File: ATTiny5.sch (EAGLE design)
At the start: 20 parts, among them Q1 BSP100, U1 SPX5205M5-L-3-3, U2 ATTINY5-TSHR, X1 DIODES, X2 INPUT

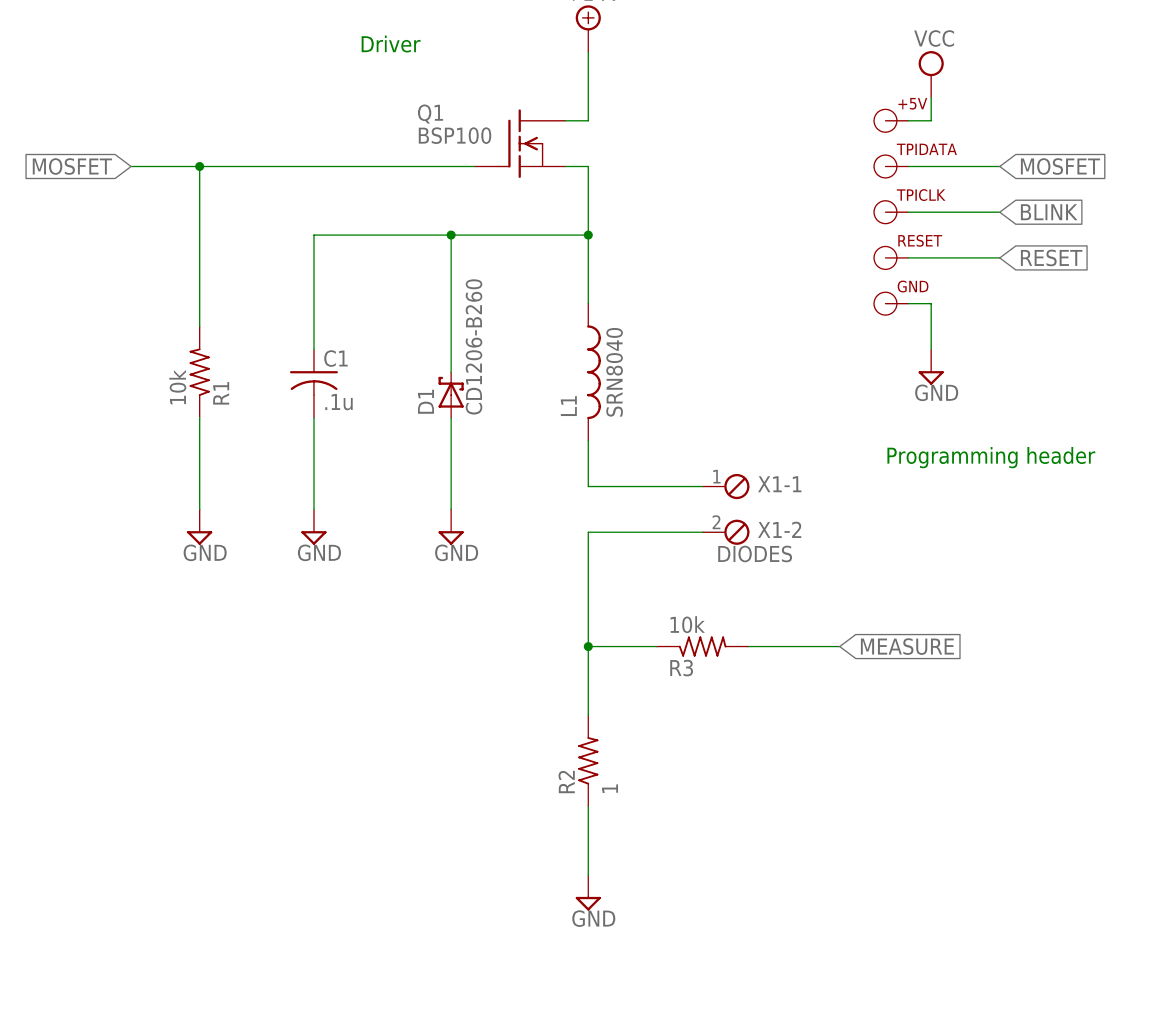
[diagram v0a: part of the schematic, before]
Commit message: Updated Board
Updated Board with Optional current limiting transistor and properly
sized and connected output cap.
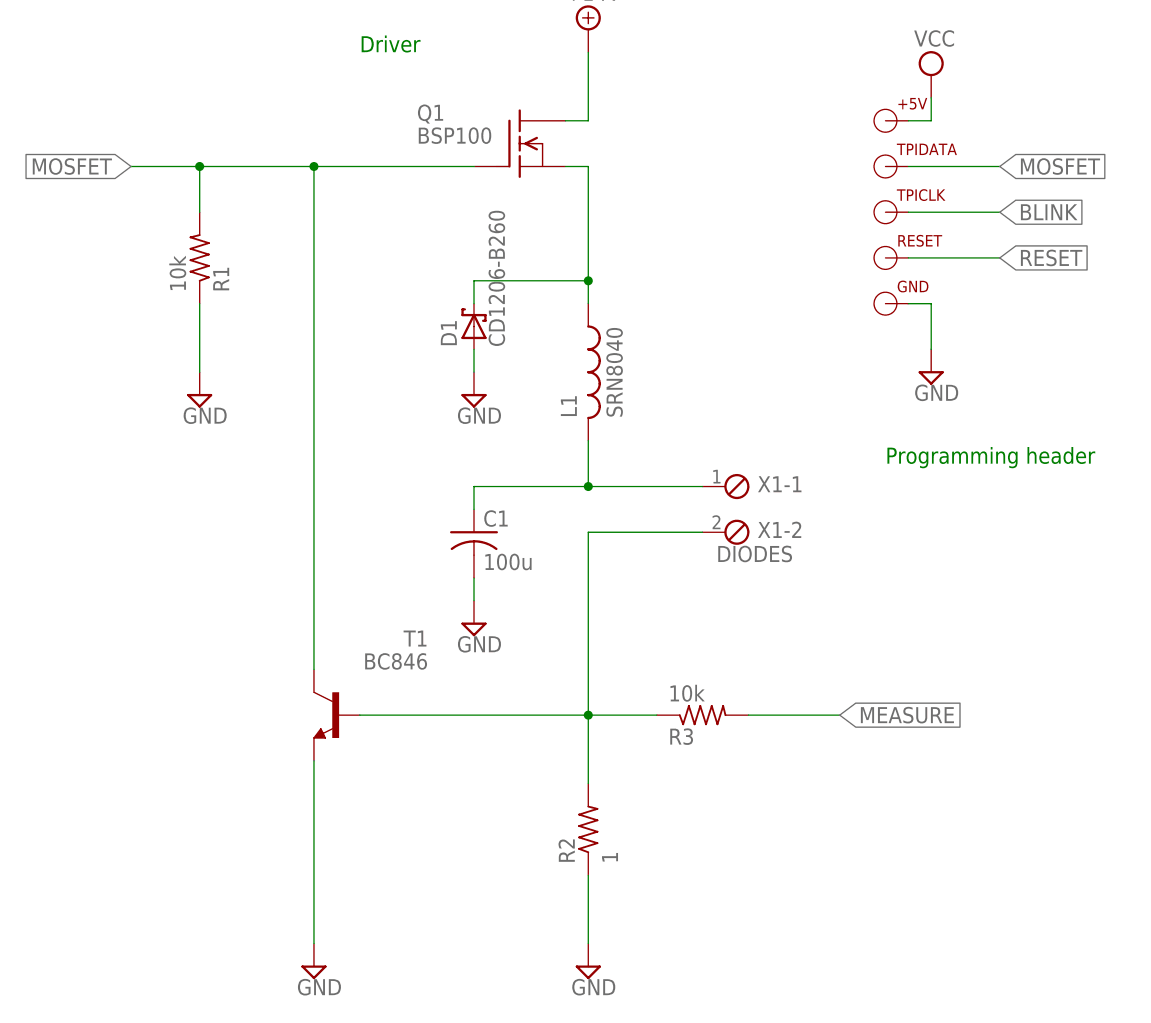
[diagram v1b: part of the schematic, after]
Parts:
- added T1: BC846, transistor:BC846
- C1: value .1u -> 100u; device resistor:C-USC0805 -> Personal:AVE107M25X16T-F
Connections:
- net D-: now also T1.B
- net GND: now also C1.C-, T1.E; no longer C1.2
- net L+: no longer C1.1
- net MOSFET: now also T1.C
- net N$3: now also C1.C+
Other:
- moved on the sheet: C1, D1, R1, R2, R3
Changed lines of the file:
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@@
 <part name="SUPPLY10" library="supply2" deviceset="GND" device=""/>
 <part name="SUPPLY12" library="supply2" deviceset="GND" device=""/>
-<part name="C1" library="resistor" deviceset="C-US" device="C0805" value=".1u"/>
+<part name="C1" library="Personal" deviceset="AVE107M25X16T-F" device="" value="100u"/>
 <part name="SUPPLY13" library="supply2" deviceset="GND" device=""/>
 <part name="R1" library="resistor" deviceset="R-US_" device="R1206" value="10k"/>
@@
 <part name="SUPPLY17" library="supply2" deviceset="GND" device=""/>
 <part name="RESET" library="Personal" deviceset="TPI" device=""/>
+<part name="T1" library="transistor" deviceset="BC846" device=""/>
+<part name="SUPPLY18" library="supply2" deviceset="GND" device=""/>
 </parts>
 <sheets>
@@
 <instance part="SUPPLY6" gate="G$1" x="139.7" y="165.1"/>
 <instance part="SUPPLY7" gate="GND" x="139.7" y="147.32"/>
-<instance part="R2" gate="G$1" x="81.28" y="33.02" rot="R90"/>
-<instance part="SUPPLY8" gate="GND" x="81.28" y="17.78"/>
+<instance part="R2" gate="G$1" x="81.28" y="25.4" rot="R90"/>
+<instance part="SUPPLY8" gate="GND" x="81.28" y="10.16"/>
 <instance part="X1" gate="-1" x="96.52" y="63.5"/>
 <instance part="X1" gate="-2" x="96.52" y="58.42"/>
@@
 <instance part="SUPPLY11" gate="G$1" x="81.28" y="114.3"/>
 <instance part="U2" gate="A" x="170.18" y="160.02"/>
-<instance part="R3" gate="G$1" x="93.98" y="45.72" rot="MR180"/>
+<instance part="R3" gate="G$1" x="93.98" y="38.1" rot="MR180"/>
 <instance part="L1" gate="G$1" x="81.28" y="76.2"/>
-<instance part="D1" gate="G$1" x="66.04" y="73.66" rot="R90"/>
+<instance part="D1" gate="G$1" x="68.58" y="81.28" rot="R90"/>
 <instance part="SUPPLY9" gate="G$1" x="43.18" y="172.72"/>
 <instance part="R4" gate="G$1" x="182.88" y="101.6" rot="R180"/>
 <instance part="R5" gate="G$1" x="195.58" y="93.98" rot="R270"/>
 <instance part="SUPPLY10" gate="GND" x="195.58" y="83.82"/>
-<instance part="SUPPLY12" gate="GND" x="66.04" y="58.42"/>
-<instance part="C1" gate="G$1" x="50.8" y="76.2"/>
-<instance part="SUPPLY13" gate="GND" x="50.8" y="58.42"/>
-<instance part="R1" gate="G$1" x="38.1" y="76.2" rot="MR90"/>
-<instance part="SUPPLY14" gate="GND" x="38.1" y="58.42"/>
+<instance part="SUPPLY12" gate="GND" x="68.58" y="73.66"/>
+<instance part="C1" gate="G$1" x="68.58" y="58.42"/>
+<instance part="SUPPLY13" gate="GND" x="68.58" y="48.26"/>
+<instance part="R1" gate="G$1" x="38.1" y="88.9" rot="MR90"/>
+<instance part="SUPPLY14" gate="GND" x="38.1" y="73.66"/>
 <instance part="TPIDATA" gate="G$1" x="114.3" y="99.06"/>
 <instance part="TPICLK" gate="G$1" x="114.3" y="93.98"/>
@@
 <instance part="SUPPLY17" gate="GND" x="33.02" y="137.16"/>
 <instance part="RESET" gate="G$1" x="114.3" y="88.9"/>
+<instance part="T1" gate="G$1" x="53.34" y="38.1" rot="MR0"/>
+<instance part="SUPPLY18" gate="GND" x="50.8" y="10.16"/>
 </instances>
 <busses>
@@
 <segment>
 <pinref part="R2" gate="G$1" pin="1"/>
-<wire x1="81.28" y1="27.94" x2="81.28" y2="20.32" width="0.1524" layer="91"/>
+<wire x1="81.28" y1="20.32" x2="81.28" y2="12.7" width="0.1524" layer="91"/>
 <pinref part="SUPPLY8" gate="GND" pin="GND"/>
 </segment>
@@
 <segment>
 <pinref part="D1" gate="G$1" pin="A"/>
-<wire x1="66.04" y1="71.12" x2="66.04" y2="60.96" width="0.1524" layer="91"/>
+<wire x1="68.58" y1="78.74" x2="68.58" y2="76.2" width="0.1524" layer="91"/>
 <pinref part="SUPPLY12" gate="GND" pin="GND"/>
 </segment>
 <segment>
 <pinref part="SUPPLY13" gate="GND" pin="GND"/>
-<pinref part="C1" gate="G$1" pin="2"/>
-<wire x1="50.8" y1="60.96" x2="50.8" y2="71.12" width="0.1524" layer="91"/>
+<pinref part="C1" gate="G$1" pin="C-"/>
+<wire x1="68.58" y1="50.8" x2="68.58" y2="53.34" width="0.1524" layer="91"/>
 </segment>
 <segment>
 <pinref part="R1" gate="G$1" pin="1"/>
 <pinref part="SUPPLY14" gate="GND" pin="GND"/>
-<wire x1="38.1" y1="71.12" x2="38.1" y2="60.96" width="0.1524" layer="91"/>
+<wire x1="38.1" y1="83.82" x2="38.1" y2="76.2" width="0.1524" layer="91"/>
 </segment>
 <segment>
@@
 <pinref part="SUPPLY17" gate="GND" pin="GND"/>
 <wire x1="33.02" y1="142.24" x2="33.02" y2="139.7" width="0.1524" layer="91"/>
+</segment>
+<segment>
+<pinref part="T1" gate="G$1" pin="E"/>
+<pinref part="SUPPLY18" gate="GND" pin="GND"/>
+<wire x1="50.8" y1="33.02" x2="50.8" y2="12.7" width="0.1524" layer="91"/>
 </segment>
 </net>
@@
 <wire x1="93.98" y1="58.42" x2="81.28" y2="58.42" width="0.1524" layer="91"/>
 <pinref part="R2" gate="G$1" pin="2"/>
-<wire x1="81.28" y1="45.72" x2="81.28" y2="38.1" width="0.1524" layer="91"/>
-<wire x1="88.9" y1="45.72" x2="81.28" y2="45.72" width="0.1524" layer="91"/>
+<wire x1="81.28" y1="38.1" x2="81.28" y2="30.48" width="0.1524" layer="91"/>
+<wire x1="88.9" y1="38.1" x2="81.28" y2="38.1" width="0.1524" layer="91"/>
 <pinref part="R3" gate="G$1" pin="1"/>
-<wire x1="81.28" y1="58.42" x2="81.28" y2="45.72" width="0.1524" layer="91"/>
-<junction x="81.28" y="45.72"/>
+<wire x1="81.28" y1="58.42" x2="81.28" y2="38.1" width="0.1524" layer="91"/>
+<junction x="81.28" y="38.1"/>
+<pinref part="T1" gate="G$1" pin="B"/>
+<wire x1="55.88" y1="38.1" x2="81.28" y2="38.1" width="0.1524" layer="91"/>
 </segment>
 </net>
@@
 <segment>
 <pinref part="R3" gate="G$1" pin="2"/>
-<wire x1="99.06" y1="45.72" x2="109.22" y2="45.72" width="0.1524" layer="91"/>
-<label x="109.22" y="45.72" size="1.778" layer="95" rot="MR180" xref="yes"/>
+<wire x1="99.06" y1="38.1" x2="109.22" y2="38.1" width="0.1524" layer="91"/>
+<label x="109.22" y="38.1" size="1.778" layer="95" rot="MR180" xref="yes"/>
 </segment>
 <segment>
@@
 <segment>
 <pinref part="Q1" gate="G$1" pin="G"/>
-<wire x1="68.58" y1="99.06" x2="38.1" y2="99.06" width="0.1524" layer="91"/>
+<wire x1="68.58" y1="99.06" x2="50.8" y2="99.06" width="0.1524" layer="91"/>
 <label x="30.48" y="99.06" size="1.778" layer="95" rot="R180" xref="yes"/>
 <pinref part="R1" gate="G$1" pin="2"/>
+<wire x1="50.8" y1="99.06" x2="38.1" y2="99.06" width="0.1524" layer="91"/>
 <wire x1="38.1" y1="99.06" x2="30.48" y2="99.06" width="0.1524" layer="91"/>
-<wire x1="38.1" y1="81.28" x2="38.1" y2="99.06" width="0.1524" layer="91"/>
+<wire x1="38.1" y1="93.98" x2="38.1" y2="99.06" width="0.1524" layer="91"/>
 <junction x="38.1" y="99.06"/>
+<pinref part="T1" gate="G$1" pin="C"/>
+<wire x1="50.8" y1="43.18" x2="50.8" y2="99.06" width="0.1524" layer="91"/>
+<junction x="50.8" y="99.06"/>
 </segment>
 <segment>
@@
 <segment>
 <pinref part="D1" gate="G$1" pin="C"/>
-<wire x1="66.04" y1="76.2" x2="66.04" y2="91.44" width="0.1524" layer="91"/>
-<wire x1="66.04" y1="91.44" x2="81.28" y2="91.44" width="0.1524" layer="91"/>
+<wire x1="68.58" y1="83.82" x2="68.58" y2="86.36" width="0.1524" layer="91"/>
+<wire x1="68.58" y1="86.36" x2="81.28" y2="86.36" width="0.1524" layer="91"/>
 <pinref part="Q1" gate="G$1" pin="S"/>
 <wire x1="78.74" y1="99.06" x2="81.28" y2="99.06" width="0.1524" layer="91"/>
-<wire x1="81.28" y1="99.06" x2="81.28" y2="91.44" width="0.1524" layer="91"/>
-<pinref part="C1" gate="G$1" pin="1"/>
-<wire x1="50.8" y1="78.74" x2="50.8" y2="91.44" width="0.1524" layer="91"/>
-<wire x1="50.8" y1="91.44" x2="66.04" y2="91.44" width="0.1524" layer="91"/>
-<junction x="66.04" y="91.44"/>
+<wire x1="81.28" y1="99.06" x2="81.28" y2="86.36" width="0.1524" layer="91"/>
 <pinref part="L1" gate="G$1" pin="1"/>
-<wire x1="81.28" y1="83.82" x2="81.28" y2="91.44" width="0.1524" layer="91"/>
-<junction x="81.28" y="91.44"/>
+<wire x1="81.28" y1="83.82" x2="81.28" y2="86.36" width="0.1524" layer="91"/>
+<junction x="81.28" y="86.36"/>
 </segment>
 </net>
@@
 <pinref part="L1" gate="G$1" pin="2"/>
 <wire x1="81.28" y1="68.58" x2="81.28" y2="63.5" width="0.1524" layer="91"/>
-</segment>
-</net>
+<pinref part="C1" gate="G$1" pin="C+"/>
+<wire x1="68.58" y1="60.96" x2="68.58" y2="63.5" width="0.1524" layer="91"/>
+<wire x1="68.58" y1="63.5" x2="81.28" y2="63.5" width="0.1524" layer="91"/>
+<junction x="81.28" y="63.5"/>
+</segment>
+</net>
